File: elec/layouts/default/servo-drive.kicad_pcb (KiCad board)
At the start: 4 copper layers, 37.5 x 39.9 mm, 133 parts, among them U2 8Mhz

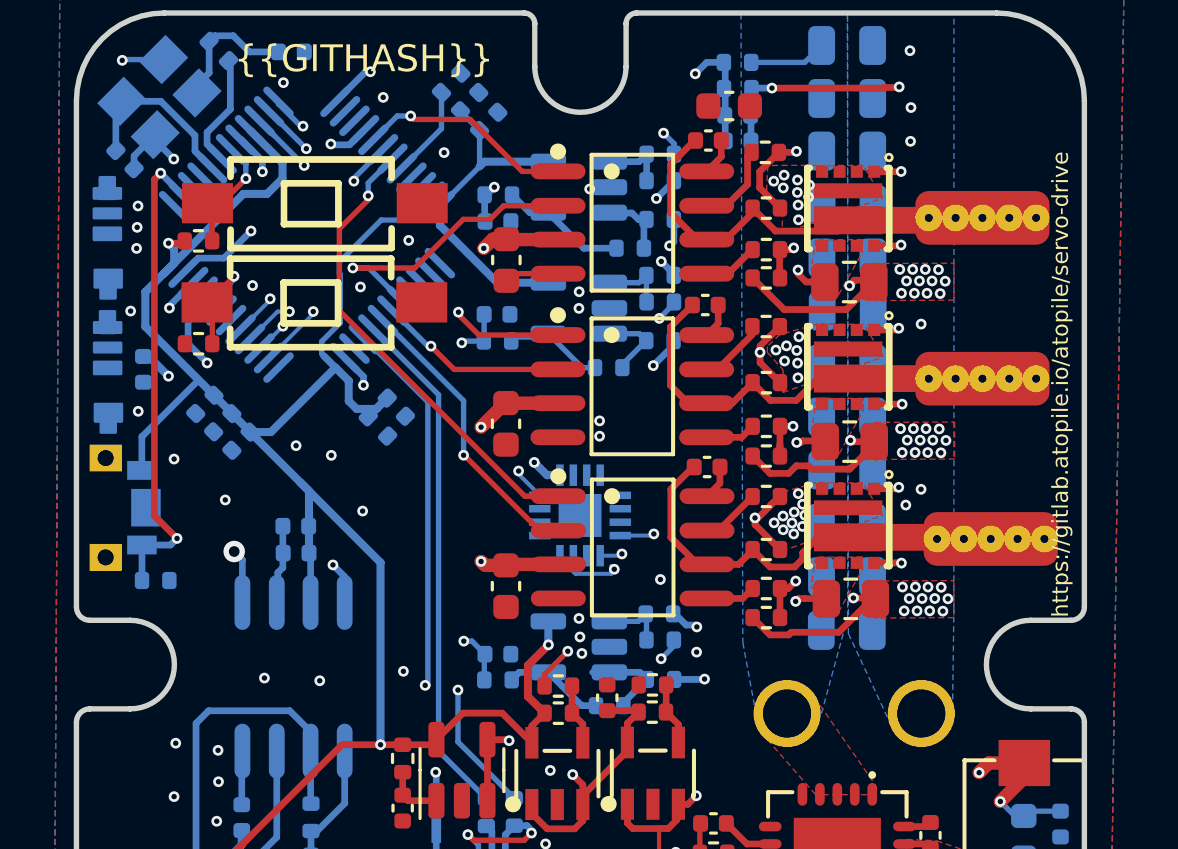
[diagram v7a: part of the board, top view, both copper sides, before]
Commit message: added JTAG with Tag connect interface, moved pos sensor to SPI2
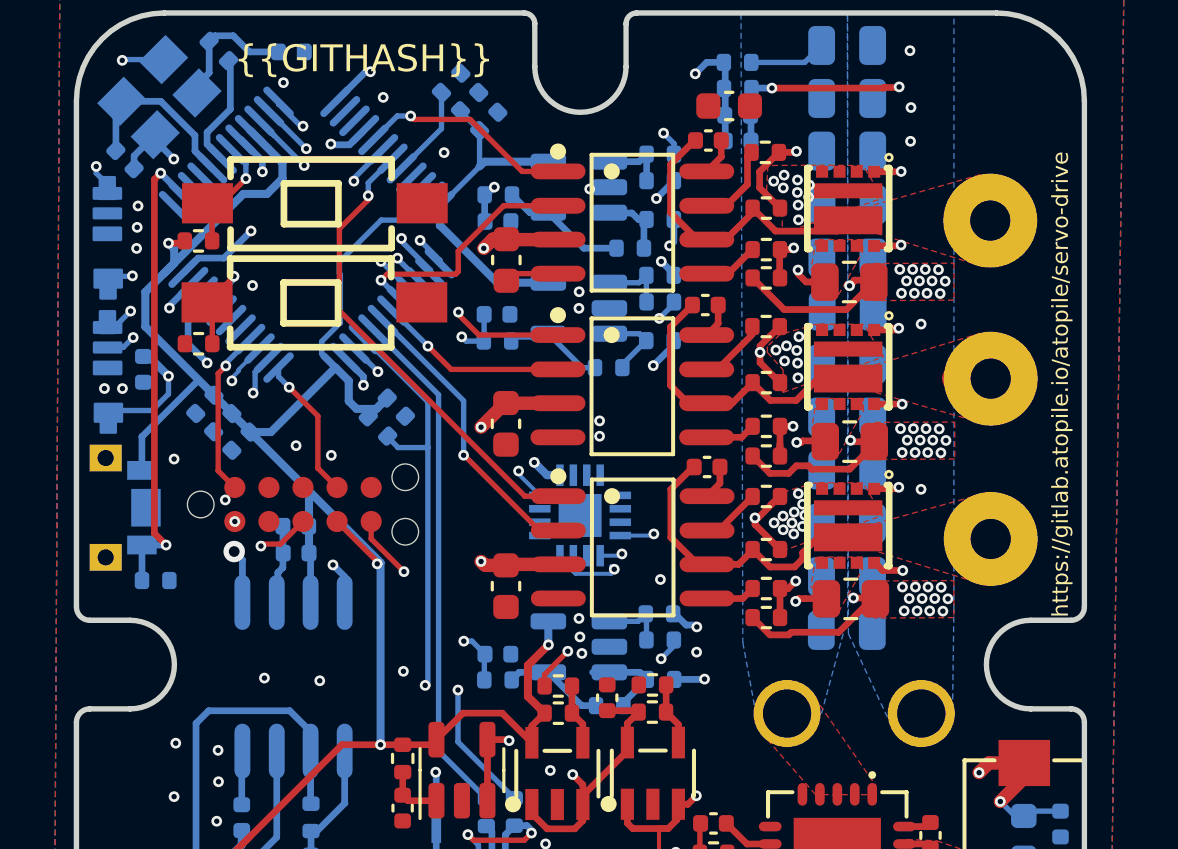
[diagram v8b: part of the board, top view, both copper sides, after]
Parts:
- added U34: , lib:TAG-CONNECT_TC2050-IDC, F.Cu at (213.4, 99.9)
- moved U8 0.31 mm to (239.0, 95.3)
- moved U7 0.31 mm to (239.0, 89.4)
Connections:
- net servo_drive.ato:ServoDrive.buck.SGND renamed buck-SGND
- net servo_drive.ato:ServoDrive.buck.buck_converter.BST renamed buck-BST
- net servo_drive.ato:ServoDrive.buck.buck_converter.CF renamed buck_converter-CF-1
- net servo_drive.ato:ServoDrive.buck.buck_converter.FB-fb_vdiv.output renamed buck-FB
- net servo_drive.ato:ServoDrive.buck.buck_converter.LX renamed buck-LX
- net servo_drive.ato:ServoDrive.buck.buck_converter.RESET renamed buck_converter-RESET-1
- net servo_drive.ato:ServoDrive.buck.buck_converter.RT renamed buck_converter-RT-1
- net servo_drive.ato:ServoDrive.buck.buck_converter.SS renamed buck-SS
- net servo_drive.ato:ServoDrive.buck.buck_converter.SYNC renamed buck_converter-SYNC-1
- net servo_drive.ato:ServoDrive.buck.buck_converter.VCC renamed buck-VCC
- net servo_drive.ato:ServoDrive.canbus.CANH-canbus_conn_1.sda-canbus_conn_2.sda renamed ServoDrive-sda
- net servo_drive.ato:ServoDrive.canbus.CANL-canbus_conn_1.scl-canbus_conn_2.scl renamed ServoDrive-scl
- net servo_drive.ato:ServoDrive.canbus.can_rx renamed ServoDrive-can_rx
- net servo_drive.ato:ServoDrive.canbus.can_tx renamed ServoDrive-can_tx
- net servo_drive.ato:ServoDrive.canbus.v_mid renamed canbus-v_mid
- net servo_drive.ato:ServoDrive.gnd renamed ServoDrive-gnd
- net servo_drive.ato:ServoDrive.ldo_3v3.feedback_div.output-ldo.adj renamed ldo_3v3-adj
- net servo_drive.ato:ServoDrive.ldo_5v.feedback_div.output-ldo.adj renamed ldo_5v-adj
- net servo_drive.ato:ServoDrive.led.data_in renamed ServoDrive-data_in
- net servo_drive.ato:ServoDrive.led.data_out-led2.data_in renamed ServoDrive-data_in-1
- net servo_drive.ato:ServoDrive.led2.data_out renamed led2-data_out
- net servo_drive.ato:ServoDrive.micro_kit.micro.BOOT0 renamed micro_kit-BOOT0
- net servo_drive.ato:ServoDrive.micro_kit.micro.NRST renamed micro_kit-NRST
- net servo_drive.ato:ServoDrive.micro_kit.micro.PA11 renamed micro_kit-PA11
- net servo_drive.ato:ServoDrive.micro_kit.micro.PA12 renamed micro_kit-PA12
- net servo_drive.ato:ServoDrive.micro_kit.micro.PA4 renamed micro-PA4-1
- net servo_drive.ato:ServoDrive.micro_kit.micro.PA5 renamed micro-PA5-1
- net servo_drive.ato:ServoDrive.micro_kit.micro.PB10 renamed micro-PB10-1
- net servo_drive.ato:ServoDrive.micro_kit.micro.PB11 renamed micro-PB11-1
- net servo_drive.ato:ServoDrive.micro_kit.micro.PB2 renamed micro_kit-PB2
- net servo_drive.ato:ServoDrive.micro_kit.micro.PB6 renamed micro-PB6-1
- net servo_drive.ato:ServoDrive.micro_kit.micro.PB7 renamed micro-PB7-1
- net servo_drive.ato:ServoDrive.micro_kit.micro.PC14_OSC32_IN renamed micro-PC14_OSC32_IN-1
- net servo_drive.ato:ServoDrive.micro_kit.micro.PC15_OSC32_OUT renamed micro-PC15_OSC32_OUT-1
- net servo_drive.ato:ServoDrive.micro_kit.micro.PD0_OSC_IN-osc.in renamed micro_kit-in
- net servo_drive.ato:ServoDrive.micro_kit.micro.PD1_OSC_OUT renamed micro_kit-PD1_OSC_OUT
- net servo_drive.ato:ServoDrive.micro_kit.micro.VBAT renamed micro-VBAT-1
- net servo_drive.ato:ServoDrive.micro_kit.osc.out renamed micro_kit-out
- net servo_drive.ato:ServoDrive.micro_kit.usb_dm-usb.dm renamed ServoDrive-usb_dm
- net servo_drive.ato:ServoDrive.micro_kit.usb_dp-usb.dp renamed ServoDrive-dp
- net servo_drive.ato:ServoDrive.position_sensor.sensor.a renamed sensor-a-1
- net servo_drive.ato:ServoDrive.position_sensor.sensor.b renamed sensor-b-1
- net servo_drive.ato:ServoDrive.position_sensor.sensor.mgh renamed sensor-mgh-1
- net servo_drive.ato:ServoDrive.position_sensor.sensor.mgl renamed sensor-mgl-1
- net servo_drive.ato:ServoDrive.position_sensor.sensor.nc renamed sensor-nc-1
- net servo_drive.ato:ServoDrive.position_sensor.sensor.pwm renamed sensor-pwm-1
- net servo_drive.ato:ServoDrive.position_sensor.sensor.ssck renamed sensor-ssck-1
- net servo_drive.ato:ServoDrive.position_sensor.sensor.ssd renamed sensor-ssd-1
- net servo_drive.ato:ServoDrive.position_sensor.sensor.test renamed sensor-test-1
- net servo_drive.ato:ServoDrive.position_sensor.sensor.z renamed sensor-z-1
- net servo_drive.ato:ServoDrive.power_stage.current_sense_a.bias_div.input-nt_p.p1 renamed current_sense_a-input-2
- net servo_drive.ato:ServoDrive.power_stage.current_sense_a.bias_div.output-opamp.in_p renamed current_sense_a-output
- net servo_drive.ato:ServoDrive.power_stage.current_sense_a.feedback_div.gnd-opamp.out-output_filter.in renamed current_sense_a-in-1
- net servo_drive.ato:ServoDrive.power_stage.current_sense_a.feedback_div.input-nt_n.p1 renamed current_sense_a-p1
- net servo_drive.ato:ServoDrive.power_stage.current_sense_a.feedback_div.output-opamp.in_n renamed current_sense_a-in_n-1
- net servo_drive.ato:ServoDrive.power_stage.current_sense_a.i_in-half_bridge_a.pwr_gnd renamed power_stage-pwr_gnd
- net servo_drive.ato:ServoDrive.power_stage.current_sense_b.bias_div.input-nt_p.p1 renamed current_sense_b-p1
- net servo_drive.ato:ServoDrive.power_stage.current_sense_b.bias_div.output-opamp.in_p renamed current_sense_b-output
- net servo_drive.ato:ServoDrive.power_stage.current_sense_b.feedback_div.gnd-opamp.out-output_filter.in renamed current_sense_b-in-1
- net servo_drive.ato:ServoDrive.power_stage.current_sense_b.feedback_div.input-nt_n.p1 renamed current_sense_b-input-2
- net servo_drive.ato:ServoDrive.power_stage.current_sense_b.feedback_div.output-opamp.in_n renamed current_sense_b-in_n-1
- net servo_drive.ato:ServoDrive.power_stage.current_sense_b.i_in-half_bridge_b.pwr_gnd renamed power_stage-pwr_gnd-1
- net servo_drive.ato:ServoDrive.power_stage.current_sense_c.bias_div.input-nt_p.p1 renamed current_sense_c-input-2
- net servo_drive.ato:ServoDrive.power_stage.current_sense_c.bias_div.output-opamp.in_p renamed current_sense_c-in_p
- net servo_drive.ato:ServoDrive.power_stage.current_sense_c.feedback_div.gnd-opamp.out-output_filter.in renamed current_sense_c-in
- net servo_drive.ato:ServoDrive.power_stage.current_sense_c.feedback_div.input-nt_n.p1 renamed current_sense_c-p1
- net servo_drive.ato:ServoDrive.power_stage.current_sense_c.feedback_div.output-opamp.in_n renamed current_sense_c-in_n-1
- net servo_drive.ato:ServoDrive.power_stage.current_sense_c.i_in-half_bridge_c.pwr_gnd renamed power_stage-pwr_gnd-2
- net servo_drive.ato:ServoDrive.power_stage.half_bridge_a.fets.gate_bottom renamed half_bridge_a-gate_bottom-1
- net servo_drive.ato:ServoDrive.power_stage.half_bridge_a.fets.gate_top renamed half_bridge_a-gate_top-1
- net servo_drive.ato:ServoDrive.power_stage.half_bridge_a.gate_driver.hvg renamed half_bridge_a-hvg-1
- net servo_drive.ato:ServoDrive.power_stage.half_bridge_a.gate_driver.lvg renamed half_bridge_a-lvg-1
- net servo_drive.ato:ServoDrive.power_stage.half_bridge_a.gate_driver.vboot renamed half_bridge_a-vboot-1
- net servo_drive.ato:ServoDrive.power_stage.half_bridge_b.fets.gate_bottom renamed half_bridge_b-gate_bottom-1
- net servo_drive.ato:ServoDrive.power_stage.half_bridge_b.fets.gate_top renamed half_bridge_b-gate_top-1
- net servo_drive.ato:ServoDrive.power_stage.half_bridge_b.gate_driver.hvg renamed half_bridge_b-hvg-1
- net servo_drive.ato:ServoDrive.power_stage.half_bridge_b.gate_driver.lvg renamed half_bridge_b-lvg-1
- net servo_drive.ato:ServoDrive.power_stage.half_bridge_b.gate_driver.vboot renamed half_bridge_b-vboot-1
- net servo_drive.ato:ServoDrive.power_stage.half_bridge_c.fets.gate_bottom renamed half_bridge_c-gate_bottom-1
- net servo_drive.ato:ServoDrive.power_stage.half_bridge_c.fets.gate_top renamed half_bridge_c-gate_top-1
- net servo_drive.ato:ServoDrive.power_stage.half_bridge_c.gate_driver.hvg renamed half_bridge_c-hvg-1
- net servo_drive.ato:ServoDrive.power_stage.half_bridge_c.gate_driver.lvg renamed half_bridge_c-lvg-1
- net servo_drive.ato:ServoDrive.power_stage.half_bridge_c.gate_driver.vboot renamed half_bridge_c-vboot-1
- net servo_drive.ato:ServoDrive.power_stage.high_in_a renamed ServoDrive-high_in_a
- net servo_drive.ato:ServoDrive.power_stage.high_in_b renamed ServoDrive-high_in_b
- net servo_drive.ato:ServoDrive.power_stage.high_in_c renamed ServoDrive-high_in_c
- net servo_drive.ato:ServoDrive.power_stage.i_fb_a renamed ServoDrive-i_fb_a
- net servo_drive.ato:ServoDrive.power_stage.i_fb_b renamed ServoDrive-i_fb_b
- net servo_drive.ato:ServoDrive.power_stage.i_fb_c renamed ServoDrive-i_fb_c
- net servo_drive.ato:ServoDrive.power_stage.low_in_a renamed ServoDrive-low_in_a
- net servo_drive.ato:ServoDrive.power_stage.low_in_b renamed ServoDrive-low_in_b
- net servo_drive.ato:ServoDrive.power_stage.low_in_c renamed ServoDrive-low_in_c
- net servo_drive.ato:ServoDrive.power_stage.out_a renamed ServoDrive-out_a
- net servo_drive.ato:ServoDrive.power_stage.out_b renamed ServoDrive-out_b
- net servo_drive.ato:ServoDrive.power_stage.out_c renamed ServoDrive-out_c
- net servo_drive.ato:ServoDrive.power_stage.reference.buffer.in_p-filter.out renamed reference-in_p
- net servo_drive.ato:ServoDrive.power_stage.v_ref renamed power_stage-v_ref
- net servo_drive.ato:ServoDrive.switch.pin1 renamed ServoDrive-pin1
- net servo_drive.ato:ServoDrive.usb.cc1 renamed ServoDrive-cc1
- net servo_drive.ato:ServoDrive.usb.cc2 renamed ServoDrive-cc2
- net servo_drive.ato:ServoDrive.usb.sbu renamed usb-sbu
- net servo_drive.ato:ServoDrive.usb.vbus-usb_diode.anode renamed ServoDrive-anode
- net servo_drive.ato:ServoDrive.v_10 renamed ServoDrive-v_10
- net servo_drive.ato:ServoDrive.v_3 renamed ServoDrive-v_3
- net servo_drive.ato:ServoDrive.v_5 renamed ServoDrive-v_5
- net servo_drive.ato:ServoDrive.vbatt renamed ServoDrive-vbatt
- net servo_drive.ato:ServoDrive.voltage_input_vdiv.out renamed ServoDrive-out
- U15 pad 25: servo_drive.ato:ServoDrive.micro_kit.micro.PB12 -> ServoDrive-cs
- U15 pad 26: servo_drive.ato:ServoDrive.micro_kit.micro.PB13 -> ServoDrive-sck
- U15 pad 27: servo_drive.ato:ServoDrive.micro_kit.micro.PB14 -> ServoDrive-miso
- U15 pad 28: servo_drive.ato:ServoDrive.micro_kit.micro.PB15 -> ServoDrive-mosi
- U15 pad 34: servo_drive.ato:ServoDrive.micro_kit.micro.PA13 -> ServoDrive-tms
- U15 pad 37: servo_drive.ato:ServoDrive.micro_kit.micro.PA14 -> ServoDrive-tck
- U15 pad 38: servo_drive.ato:ServoDrive.position_sensor.cs -> ServoDrive-tdi
- U15 pad 39: servo_drive.ato:ServoDrive.position_sensor.sck -> ServoDrive-tdo
- U15 pad 40: servo_drive.ato:ServoDrive.position_sensor.miso -> ServoDrive-rst
- U15 pad 41: servo_drive.ato:ServoDrive.position_sensor.mosi -> micro-PB5-1
- U18 pad 12: servo_drive.ato:ServoDrive.position_sensor.sck -> ServoDrive-sck
- U18 pad 4: servo_drive.ato:ServoDrive.position_sensor.mosi -> ServoDrive-mosi
- U18 pad 5: servo_drive.ato:ServoDrive.position_sensor.cs -> ServoDrive-cs
- U18 pad 7: servo_drive.ato:ServoDrive.position_sensor.miso -> ServoDrive-miso
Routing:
- net servo_drive.ato:ServoDrive.position_sensor.miso: track 21.6 -> 0.00 mm, vias 2 -> 0
- net ServoDrive-miso: track 0.00 -> 21.4 mm, vias 0 -> 2
- net servo_drive.ato:ServoDrive.position_sensor.mosi: track 20.8 -> 0.00 mm, vias 2 -> 0
- net servo_drive.ato:ServoDrive.position_sensor.cs: track 19.4 -> 0.00 mm, vias 2 -> 0
- net ServoDrive-cs: track 0.00 -> 18.9 mm, vias 0 -> 2
- net ServoDrive-mosi: track 0.00 -> 17.7 mm, vias 0 -> 2
- net ServoDrive-sck: track 0.00 -> 16.0 mm, vias 0 -> 2
- net servo_drive.ato:ServoDrive.position_sensor.sck: track 14.2 -> 0.00 mm, vias 2 -> 0
- net ServoDrive-tms: track 0.00 -> 11.7 mm, vias 0 -> 2
- net ServoDrive-v_5: track 39.2 -> 48.6 mm, vias 3 -> 4
- net ServoDrive-tdi: track 0.00 -> 9.32 mm, vias 0 -> 2
- net ServoDrive-data_in-1: track 0.00 -> 9.18 mm, vias 0 -> 2
- net (no net): track 0.00 -> 8.44 mm
- net current_sense_a-input-2: track 7.88 -> 0.00 mm
- net ServoDrive-tdo: track 0.00 -> 7.05 mm, vias 0 -> 2
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- added copper zone on F.Cu, net ServoDrive-out_a
- added copper zone on F.Cu, net ServoDrive-out_b
- added copper zone on F.Cu, net ServoDrive-out_c
